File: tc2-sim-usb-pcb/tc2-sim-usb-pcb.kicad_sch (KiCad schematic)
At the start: 9 parts, among them J11 Conn_01x08

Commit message: P3-Nov release
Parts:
- added H3: MountingHole, cacophony-library:mouse-bite-10mm, symbol Mechanical:MountingHole
- H1, H2: footprint MountingHole:MountingHole_2.7mm_M2.5 -> cacophony-library:MountingHole_2.7mm_M2.5
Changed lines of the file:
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@@
+    )
+  )
+  (global_label "Zip tie" (shape input) (at 82.55 43.18 0) (fields_autoplaced)
+    (effects (font (size 1.27 1.27)) (justify left))
+    (property "Intersheetrefs" "${INTERSHEET_REFS}" (at 91.8852 43.18 0)
+      (effects (font (size 1.27 1.27)) (justify left) hide)
     )
   )
@@
       (effects (font (size 1.27 1.27)) (justify left))
     )
-    (property "Footprint" "MountingHole:MountingHole_2.7mm_M2.5" (at 110.49 127 0)
+    (property "Footprint" "cacophony-library:MountingHole_2.7mm_M2.5" (at 110.49 127 0)
       (effects (font (size 1.27 1.27)) hide)
     )
@@
     )
   )
+  (symbol (lib_id "Mechanical:MountingHole") (at 161.29 72.39 0) (unit 1)
+    (in_bom yes) (on_board yes) (dnp no) (fields_autoplaced)
+    (property "Reference" "H3" (at 163.83 71.12 0)
+      (effects (font (size 1.27 1.27)) (justify left))
+    )
+    (property "Value" "MountingHole" (at 163.83 73.66 0)
+      (effects (font (size 1.27 1.27)) (justify left))
+    )
+    (property "Footprint" "cacophony-library:mouse-bite-10mm" (at 161.29 72.39 0)
+      (effects (font (size 1.27 1.27)) hide)
+    )
+    (property "Datasheet" "~" (at 161.29 72.39 0)
+      (effects (font (size 1.27 1.27)) hide)
+    )
+    (instances
+      (project "tc2-sim-usb-pcb"
+        (path "/12797a05-1f89-472c-86ab-484e34ff8b5b"
+          (reference "H3") (unit 1)
+        )
+      )
+    )
+  )
   (symbol (lib_id "cacophony-library:SIM-Nano") (at 118.11 91.44 0) (unit 1)
     (in_bom yes) (on_board yes) (dnp no) (fields_autoplaced)
@@
       (effects (font (size 1.27 1.27)) (justify left))
     )
-    (property "Footprint" "MountingHole:MountingHole_2.7mm_M2.5" (at 110.49 133.35 0)
-      (effects (font (size 1.27 1.27)) hide)
-    )
+    (property "Footprint" "cacophony-library:MountingHole_2.7mm_M2.5" (at 110.49 133.35 0)
+      (effects (font (size 1.27 1.27)) hide)
+    )

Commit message: v0.4.0
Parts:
- added U1, U2: ~, cacophony-library:ziptie, symbol cacophony-library:ziptie

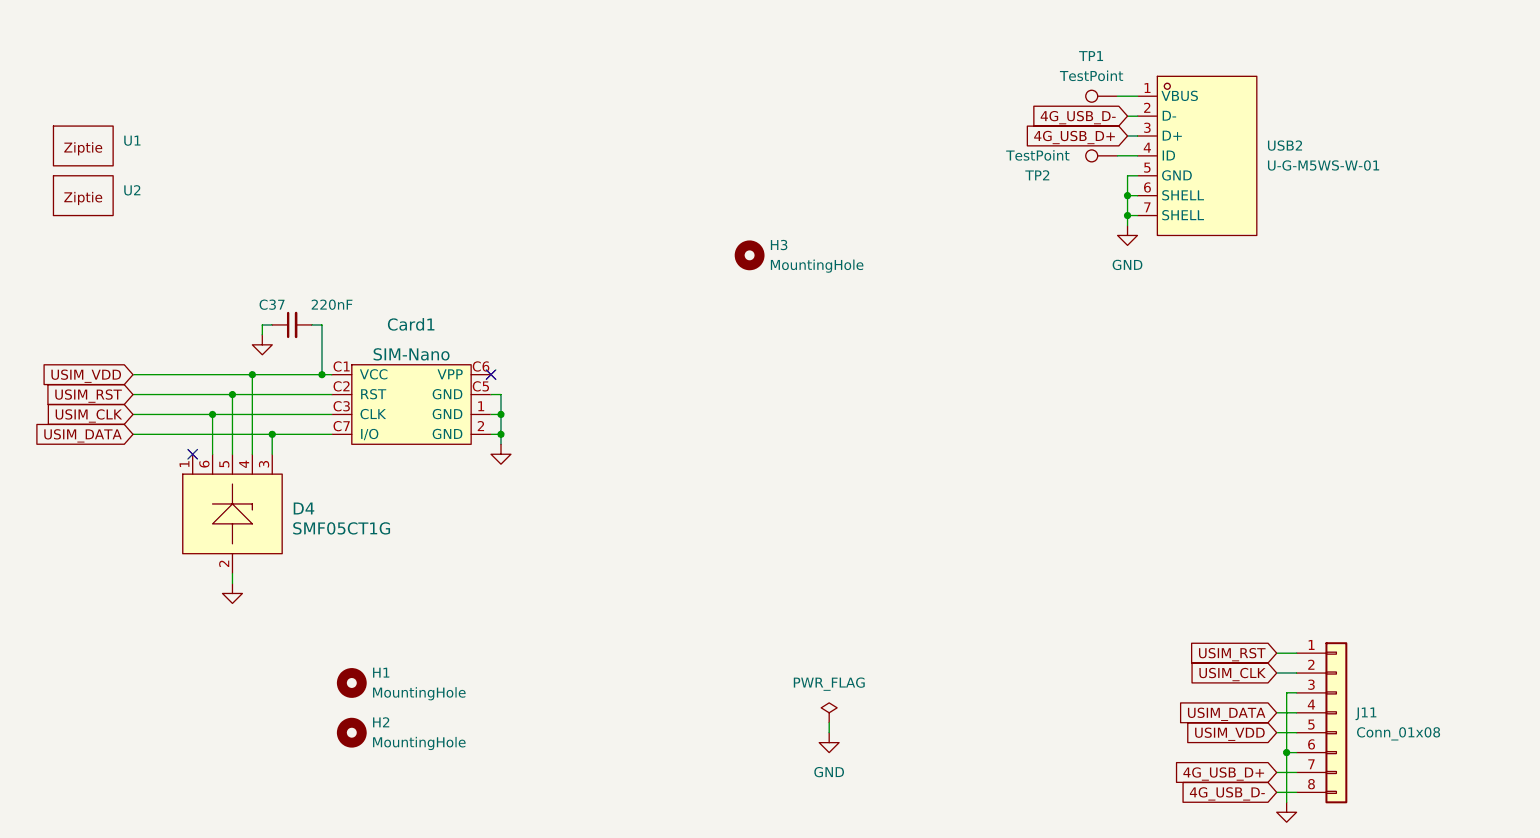
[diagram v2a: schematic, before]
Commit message: Change to through hole connector and add simcard PCB to pannel
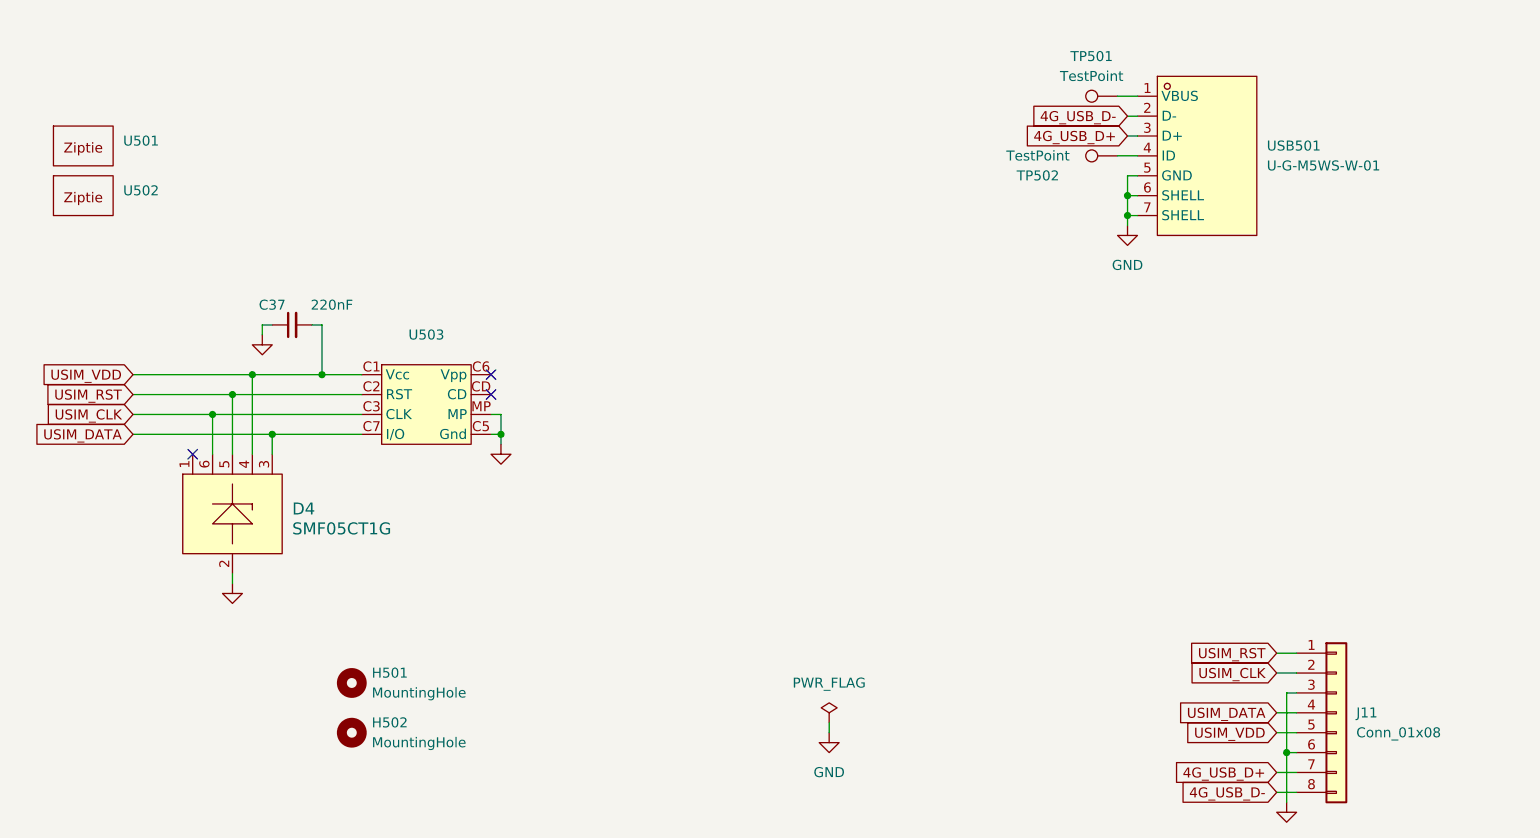
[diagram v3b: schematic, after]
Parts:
- removed Card1: SIM-Nano, cacophony-library:SIM-SMD_SMN-304, symbol cacophony-library:SIM-Nano
- removed H3: MountingHole, cacophony-library:mouse-bite-10mm, symbol Mechanical:MountingHole
- added U503: ~, cacophony-library:K-DYX-010, symbol cacophony-library:K-DYX-010
- renumbered H1 to H501, H2 to H502, TP1 to TP501, TP2 to TP502, U1 to U501, U2 to U502, USB2 to USB501
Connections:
- net GND: now also U503.C5 (Gnd), U503.MP, U503.MP_2 (MP), U503.MP_3 (MP), U503.MP_4 (MP)
- net USIM_CLK: now also U503.C3 (CLK)
- net USIM_DATA: now also U503.C7 (I/O)
- net USIM_RST: now also U503.C2 (RST)
- net USIM_VDD: now also U503.C1 (Vcc)
- no-connect marks 2 -> 3

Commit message: Version v0.7.0
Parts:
- removed TP501, TP502: TestPoint, TestPoint:TestPoint_Pad_D2.0mm, symbol Connector:TestPoint
- J11: now left out of the parts list
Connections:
- no-connect marks 3 -> 5
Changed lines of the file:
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@@
+	)
+	(no_connect
+		(at 210.82 52.07)
 	)
 	(no_connect
@@
 		(at 128.27 90.17)
 	)
+	(no_connect
+		(at 210.82 59.69)
+	)
 	(wire
 		(pts
@@
 	(wire
 		(pts
-			(xy 208.28 59.69) (xy 210.82 59.69)
-		)
-		(stroke
-			(width 0)
-			(type default)
-		)
-	)
-	(wire
-		(pts
 			(xy 209.55 68.58) (xy 209.55 67.31)
 		)
@@
 		(pts
 			(xy 82.55 92.71) (xy 92.71 92.71)
-		)
-		(stroke
-			(width 0)
-			(type default)
-		)
-	)
-	(wire
-		(pts
-			(xy 208.28 52.07) (xy 210.82 52.07)
 		)
 		(stroke
@@
 	)
 	(symbol
-		(lib_id "Connector:TestPoint")
-		(at 208.28 59.69 90)
-		(unit 1)
-		(exclude_from_sim no)
-		(in_bom yes)
-		(on_board yes)
-		(dnp no)
-		(property "Reference" "TP502"
-			(at 198.12 62.23 90)
-			(effects
-				(font
-					(size 1.27 1.27)
-				)
-			)
-		)
-		(property "Value" "TestPoint"
-			(at 198.12 59.69 90)
-			(effects
-				(font
-					(size 1.27 1.27)
-				)
-			)
-		)
-		(property "Footprint" "TestPoint:TestPoint_Pad_D2.0mm"
-			(at 208.28 54.61 0)
-			(effects
-				(font
-					(size 1.27 1.27)
-				)
-				(hide yes)
-			)
-		)
-		(property "Datasheet" "~"
-			(at 208.28 54.61 0)
-			(effects
-				(font
-					(size 1.27 1.27)
-				)
-				(hide yes)
-			)
-		)
-		(property "Description" ""
-			(at 208.28 59.69 0)
-			(effects
-				(font
-					(size 1.27 1.27)
-				)
-				(hide yes)
-			)
-		)
-		(pin "1"
-		)
-		(instances
-			(project "tc2-sim-usb-pcb"
-				(path "/12797a05-1f89-472c-86ab-484e34ff8b5b"
-					(reference "TP502")
-					(unit 1)
-				)
-			)
-		)
-	)
-	(symbol
 		(lib_id "power:GND")
 		(at 99.06 82.55 0)
@@
 	)
 	(symbol
-		(lib_id "Connector:TestPoint")
-		(at 208.28 52.07 90)
-		(unit 1)
-		(exclude_from_sim no)
-		(in_bom yes)
-		(on_board yes)
-		(dnp no)
-		(fields_autoplaced yes)
-		(property "Reference" "TP501"
-			(at 204.978 46.99 90)
-			(effects
-				(font
-					(size 1.27 1.27)
-				)
-			)
-		)
-		(property "Value" "TestPoint"
-			(at 204.978 49.53 90)
-			(effects
-				(font
-					(size 1.27 1.27)
-				)
-			)
-		)
-		(property "Footprint" "TestPoint:TestPoint_Pad_D2.0mm"
-			(at 208.28 46.99 0)
-			(effects
-				(font
-					(size 1.27 1.27)
-				)
-				(hide yes)
-			)
-		)
-		(property "Datasheet" "~"
-			(at 208.28 46.99 0)
-			(effects
-				(font
-					(size 1.27 1.27)
-				)
-				(hide yes)
-			)
-		)
-		(property "Description" ""
-			(at 208.28 52.07 0)
-			(effects
-				(font
-					(size 1.27 1.27)
-				)
-				(hide yes)
-			)
-		)
-		(pin "1"
-		)
-		(instances
-			(project "tc2-sim-usb-pcb"
-				(path "/12797a05-1f89-472c-86ab-484e34ff8b5b"
-					(reference "TP501")
-					(unit 1)
-				)
-			)
-		)
-	)
-	(symbol
 		(lib_id "Connector_Generic:Conn_01x08")
 		(at 236.22 130.81 0)
 		(unit 1)
 		(exclude_from_sim no)
-		(in_bom yes)
+		(in_bom no)
 		(on_board yes)
 		(dnp no)

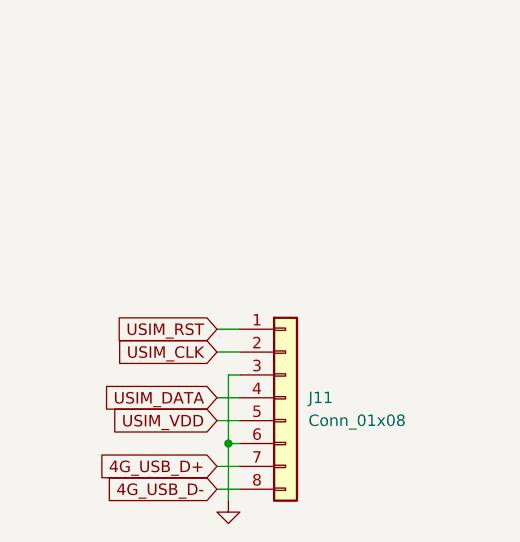
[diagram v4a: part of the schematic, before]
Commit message: v0.7.2 panelise microphone boards
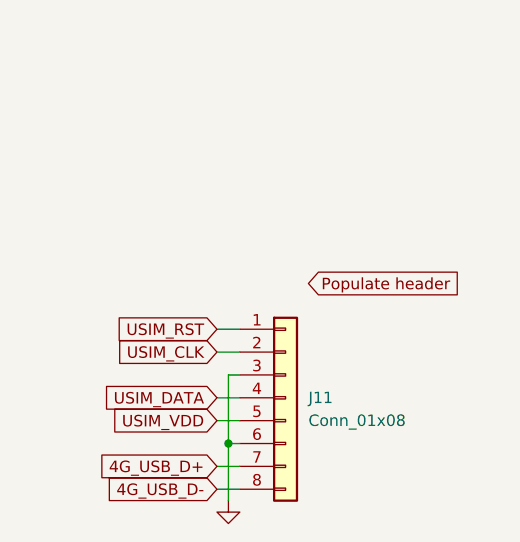
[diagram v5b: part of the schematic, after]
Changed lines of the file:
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@@
+		)
+	)
+	(global_label "Populate header"
+		(shape input)
+		(at 238.76 118.11 0)
+		(fields_autoplaced yes)
+		(effects
+			(font
+				(size 1.27 1.27)
+			)
+			(justify left)
+		)
+		(property "Intersheetrefs" "${INTERSHEET_REFS}"
+			(at 257.4687 118.11 0)
+			(effects
+				(font
+					(size 1.27 1.27)
+				)
+				(justify left)
+				(hide yes)
+			)
 		)
 	)

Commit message: v0.7.3
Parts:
- J11: LCSC (none) -> C5156616; now not fitted
- USB501: LCSC (none) -> C283546; LCSC Part C283546 -> (none)
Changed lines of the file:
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@@
 	(wire
 		(pts
-			(xy 171.45 132.08) (xy 171.45 133.35)
+			(xy 205.74 128.27) (xy 205.74 129.54)
 		)
 		(stroke
@@
 				)
 				(justify right)
-				(hide yes)
-			)
-		)
-	)
-	(global_label "Populate header"
-		(shape input)
-		(at 238.76 118.11 0)
-		(fields_autoplaced yes)
-		(effects
-			(font
-				(size 1.27 1.27)
-			)
-			(justify left)
-		)
-		(property "Intersheetrefs" "${INTERSHEET_REFS}"
-			(at 257.4687 118.11 0)
-			(effects
-				(font
-					(size 1.27 1.27)
-				)
-				(justify left)
 				(hide yes)
 			)
@@
 	(symbol
 		(lib_id "power:GND")
-		(at 171.45 133.35 0)
+		(at 205.74 129.54 0)
 		(unit 1)
 		(exclude_from_sim no)
@@
 		(fields_autoplaced yes)
 		(property "Reference" "#PWR0505"
-			(at 171.45 139.7 0)
+			(at 205.74 135.89 0)
 			(effects
 				(font
@@
 		)
 		(property "Value" "GND"
-			(at 171.45 138.43 0)
-			(effects
-				(font
-					(size 1.27 1.27)
-				)
+			(at 205.74 134.62 0)
+			(effects
+				(font
+					(size 1.27 1.27)
+				)
+				(hide yes)
 			)
 		)
 		(property "Footprint" ""
-			(at 171.45 133.35 0)
+			(at 205.74 129.54 0)
 			(effects
 				(font
@@
 		)
 		(property "Datasheet" ""
-			(at 171.45 133.35 0)
+			(at 205.74 129.54 0)
 			(effects
 				(font
@@
 		)
 		(property "Description" "Power symbol creates a global label with name \"GND\" , ground"
-			(at 171.45 133.35 0)
+			(at 205.74 129.54 0)
 			(effects
 				(font
@@
 		(in_bom no)
 		(on_board yes)
-		(dnp no)
+		(dnp yes)
 		(fields_autoplaced yes)
 		(property "Reference" "J11"
@@
 		)
 		(property "Description" ""
+			(at 236.22 130.81 0)
+			(effects
+				(font
+					(size 1.27 1.27)
+				)
+				(hide yes)
+			)
+		)
+		(property "LCSC" "C5156616"
 			(at 236.22 130.81 0)
 			(effects
@@
 			)
 		)
-		(property "LCSC Part" "C283546"
-			(at 219.71 77.47 0)
+		(property "LCSC" "C283546"
+			(at 219.71 59.69 0)
 			(effects
 				(font
@@
 	(symbol
 		(lib_id "power:PWR_FLAG")
-		(at 171.45 132.08 0)
+		(at 205.74 128.27 0)
 		(unit 1)
 		(exclude_from_sim no)
@@
 		(fields_autoplaced yes)
 		(property "Reference" "#FLG0501"
-			(at 171.45 130.175 0)
+			(at 205.74 126.365 0)
 			(effects
 				(font
@@
 		)
 		(property "Value" "PWR_FLAG"
-			(at 171.45 127 0)
+			(at 205.74 123.19 0)
 			(effects
 				(font
@@
 		)
 		(property "Footprint" ""
-			(at 171.45 132.08 0)
+			(at 205.74 128.27 0)
 			(effects
 				(font
@@
 		)
 		(property "Datasheet" "~"
-			(at 171.45 132.08 0)
+			(at 205.74 128.27 0)
 			(effects
 				(font
@@
 		)
 		(property "Description" "Special symbol for telling ERC where power comes from"
-			(at 171.45 132.08 0)
-			(effects
-				(font
+			(at 205.74 128.27 0)
+			(effects
+				(font

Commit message: Updated to use field LCSC Part instead of LCSC for the JLCPCB part number
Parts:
- C37: LCSC C16772 -> (none); LCSC Part (none) -> C16772
- D4: LCSC C15879 -> (none); LCSC Part (none) -> C15879
- J11: LCSC C5156616 -> (none); LCSC Part (none) -> C5156616
- U503: LCSC C2919617 -> (none); LCSC Part (none) -> C2919617
- USB501: LCSC C283546 -> (none); LCSC Part (none) -> C283546
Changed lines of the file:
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@@
 			)
 		)
-		(property "LCSC" "C15879"
+		(property "LCSC Part" "C15879"
 			(at 95.25 104.14 0)
 			(effects
@@
 			)
 		)
-		(property "LCSC" "C5156616"
+		(property "LCSC Part" "C5156616"
 			(at 236.22 130.81 0)
 			(effects
@@
 			)
 		)
-		(property "LCSC" "C283546"
+		(property "LCSC Part" "C283546"
 			(at 219.71 59.69 0)
 			(effects
@@
 			)
 		)
-		(property "LCSC" "C2919617"
+		(property "LCSC Part" "C2919617"
 			(at 120.015 83.82 0)
 			(effects
@@
 			)
 		)
-		(property "LCSC" "C16772"
+		(property "LCSC Part" "C16772"
 			(at 102.87 81.28 0)
 			(effects
